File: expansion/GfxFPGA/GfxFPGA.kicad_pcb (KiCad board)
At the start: 4 copper layers, 100 x 100 mm, 3 parts, among them J1 JTAG, J101 D68K_64PIN_BOARD, J501 VGA Out

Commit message: WOrking on VGA card
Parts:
- removed J501: VGA Out, Connector_Dsub:DSUB-15-HD_Female_Horizontal_P2.29x1.98mm_EdgePinOffset3.03mm_Housed_MountingHolesOffset4.94mm
- added C1: 47uF, Capacitor_SMD:CP_Elec_4x5.3, F.Cu at (106.5, 99.5)
- added C10: 100nF, Capacitor_SMD:C_0805_2012Metric, B.Cu at (144.9, 94.3)
- added C11: 100nF, Capacitor_SMD:C_0805_2012Metric, B.Cu at (151.3, 100.7)
- added C12: 100nF, Capacitor_SMD:C_0805_2012Metric, B.Cu at (160.9, 93.4)
- added C13: 100nF, Capacitor_SMD:C_0805_2012Metric, B.Cu at (152.0, 84.7)
- added C14: 100nF, Capacitor_SMD:C_0805_2012Metric, B.Cu at (136.4, 116.3)
- added C15: 100nF, Capacitor_SMD:C_0805_2012Metric, B.Cu at (151.3, 96.4)
- added C16: 100nF, Capacitor_SMD:C_0805_2012Metric, B.Cu at (145.0, 89.4)
- added C17: 100nF, Capacitor_SMD:C_0805_2012Metric, B.Cu at (160.8, 88.6)
- added C18: 100nF, Capacitor_SMD:C_0805_2012Metric, B.Cu at (147.9, 84.8)
- added C19: 0.1uF, Capacitor_SMD:CP_Elec_4x5.3, F.Cu at (115.0, 92.9)
- added C2: 100nF, Capacitor_SMD:C_0805_2012Metric, F.Cu at (108.8, 116.6)
- added C20: 100nF, Capacitor_SMD:C_0805_2012Metric, B.Cu at (158.0, 84.7)
- added C21: 100nF, Capacitor_SMD:C_0805_2012Metric, B.Cu at (184.1, 128.7)
- added C22: 100nF, Capacitor_SMD:C_0805_2012Metric, B.Cu at (171.6, 129.1)
- added C23: 100nF, Capacitor_SMD:C_0805_2012Metric, B.Cu at (147.7, 115.8)
- added C24: 100nF, Capacitor_SMD:C_0805_2012Metric, B.Cu at (121.2, 128.8)
- added C25: 100nF, Capacitor_SMD:C_0805_2012Metric, B.Cu at (136.3, 122.7)
- added C26: 100nF, Capacitor_SMD:C_0805_2012Metric, B.Cu at (184.1, 132.4)
- added C27: 100nF, Capacitor_SMD:C_0805_2012Metric, B.Cu at (171.6, 132.4)
- added C28: 100nF, Capacitor_SMD:C_0805_2012Metric, B.Cu at (155.3, 129.8)
- added C29: 100nF, Capacitor_SMD:C_0805_2012Metric, B.Cu at (142.3, 129.9)
- added C3: 47uF, Capacitor_SMD:CP_Elec_4x5.3, F.Cu at (115.0, 99.6)
- added C30: 100nF, Capacitor_SMD:C_0805_2012Metric, B.Cu at (129.3, 129.8)
- added C31: 100nF, Capacitor_SMD:C_0805_2012Metric, B.Cu at (121.2, 132.7)
- added C32: 100nF, Capacitor_SMD:C_0805_2012Metric, B.Cu at (147.6, 119.6)
- added C33: 100nF, Capacitor_SMD:C_0805_2012Metric, B.Cu at (120.3, 73.0)
- added C34: 100nF, Capacitor_SMD:C_0805_2012Metric, B.Cu at (135.2, 72.9)
- added C35: 100nF, Capacitor_SMD:C_0805_2012Metric, F.Cu at (195.4, 116.3)
- added C36: 100nF, Capacitor_SMD:C_0805_2012Metric, F.Cu at (194.6, 79.7)
- added C37: 100nF, Capacitor_SMD:C_0805_2012Metric, F.Cu at (158.8, 115.9)
- added C4: 100nF, Capacitor_SMD:C_0805_2012Metric, F.Cu at (106.6, 103.4)
- added C5: 47uF, Capacitor_SMD:CP_Elec_4x5.3, F.Cu at (108.1, 123.5)
- added C6: 10uF, Capacitor_SMD:CP_Elec_4x5.3, F.Cu at (122.4, 111.8)
- added C7: 100nF, Capacitor_SMD:C_0805_2012Metric, F.Cu at (115.3, 103.4)
- added C8: 100nF, Capacitor_SMD:C_0805_2012Metric, F.Cu at (116.5, 110.0)
- added C9: 100nF, Capacitor_SMD:C_0805_2012Metric, F.Cu at (107.8, 135.6)
- added D1: LED, LED_SMD:LED_1206_3216Metric, F.Cu at (130.5, 98.7)
- added D2: LED, LED_SMD:LED_1206_3216Metric, F.Cu at (126.6, 98.7)
- added D3: LED, LED_SMD:LED_1206_3216Metric, F.Cu at (196.1, 130.6)
- added D4: LED, LED_SMD:LED_1206_3216Metric, F.Cu at (196.0, 133.6)
- added D5: LED, LED_SMD:LED_1206_3216Metric, F.Cu at (196.0, 127.6)
- added J3: DE15_Receptacle_HighDensity, Connector_Dsub:DSUB-15-HD_Female_Horizontal_P2.29x1.98mm_EdgePinOffset3.03mm_Housed_MountingHolesOffset4.94mm, F.Cu at (192.9, 93.6)
- added Q1: BC847, Package_TO_SOT_SMD:SOT-23, F.Cu at (122.4, 104.2)
- added R1: 390R, Resistor_SMD:R_0805_2012Metric, F.Cu at (126.9, 104.1)
- added R10: 0R, Resistor_SMD:R_0805_2012Metric, F.Cu at (185.1, 123.7)
- added R11: 0R, Resistor_SMD:R_0805_2012Metric, F.Cu at (168.5, 123.5)
- added R12: 0R, Resistor_SMD:R_0805_2012Metric, F.Cu at (166.1, 123.5)
- added R13: 0R, Resistor_SMD:R_0805_2012Metric, F.Cu at (192.7, 120.1)
- added R14: 10K, Resistor_SMD:R_0805_2012Metric, B.Cu at (159.8, 100.6)
- added R15: 10K, Resistor_SMD:R_0805_2012Metric, B.Cu at (155.7, 100.7)
- added R16: 10K, Resistor_SMD:R_0805_2012Metric, B.Cu at (146.7, 100.6)
- added R17: 10K, Resistor_SMD:R_0805_2012Metric, F.Cu at (108.8, 92.9)
- added R18: 390R, Resistor_SMD:R_0805_2012Metric, F.Cu at (192.7, 123.4)
- added R19: 10K, Resistor_SMD:R_0805_2012Metric, B.Cu at (164.4, 104.3)
- added R2: 390R, Resistor_SMD:R_0805_2012Metric, F.Cu at (130.4, 104.1)
- added R20: 10K, Resistor_SMD:R_0805_2012Metric, B.Cu at (180.0, 128.8)
- added R21: 499R, Resistor_SMD:R_0805_2012Metric, F.Cu at (187.5, 74.4)
- added R22: 1K, Resistor_SMD:R_0805_2012Metric, F.Cu at (187.5, 76.6)
- added R23: 2K, Resistor_SMD:R_0805_2012Metric, F.Cu at (187.5, 78.8)
- added R24: 4K, Resistor_SMD:R_0805_2012Metric, F.Cu at (187.5, 81.0)
- added R25: 8K, Resistor_SMD:R_0805_2012Metric, F.Cu at (187.5, 83.2)
- added R26: 499R, Resistor_SMD:R_0805_2012Metric, F.Cu at (187.5, 85.5)
- added R27: 1K, Resistor_SMD:R_0805_2012Metric, F.Cu at (187.5, 87.7)
- added R28: 2K, Resistor_SMD:R_0805_2012Metric, F.Cu at (187.5, 89.9)
- added R29: 4K, Resistor_SMD:R_0805_2012Metric, F.Cu at (187.5, 92.1)
- added R3: 390R, Resistor_SMD:R_0805_2012Metric, F.Cu at (122.3, 99.5)
- added R30: 8K, Resistor_SMD:R_0805_2012Metric, F.Cu at (187.5, 94.4)
- added R31: 16K, Resistor_SMD:R_0805_2012Metric, F.Cu at (187.5, 96.6)
- added R32: 499R, Resistor_SMD:R_0805_2012Metric, F.Cu at (187.4, 98.9)
- added R33: 1K, Resistor_SMD:R_0805_2012Metric, F.Cu at (187.4, 101.1)
- added R34: 2K, Resistor_SMD:R_0805_2012Metric, F.Cu at (187.4, 103.4)
- added R35: 4K, Resistor_SMD:R_0805_2012Metric, F.Cu at (187.4, 105.6)
- added R36: 8K, Resistor_SMD:R_0805_2012Metric, F.Cu at (187.3, 107.9)
- added R37: 82.5R, Resistor_SMD:R_0805_2012Metric, F.Cu at (187.4, 110.1)
- added R38: 82.5R, Resistor_SMD:R_0805_2012Metric, F.Cu at (187.4, 112.2)
- added R4: 120R, Resistor_SMD:R_0805_2012Metric, F.Cu at (116.6, 113.4)
- added R5: 390R, Resistor_SMD:R_0805_2012Metric, F.Cu at (196.7, 120.1)
- added R6: 390R, Resistor_SMD:R_0805_2012Metric, F.Cu at (196.6, 123.4)
- added R7: 10K, Resistor_SMD:R_0805_2012Metric, B.Cu at (132.3, 112.2)
- added R8: 10K, Resistor_SMD:R_0805_2012Metric, B.Cu at (136.8, 112.2)
- added R9: 10K, Resistor_SMD:R_0805_2012Metric, B.Cu at (141.4, 112.2)
- added U1: SN74LS125ADR, Package_SO:SO-14_3.9x8.65mm_P1.27mm, F.Cu at (110.7, 130.5)
- added U10: SN74LVC8T245PWR, Ddraig:SOP65P640X120-24N, F.Cu at (121.2, 130.3)
- added U11: SN74LVC8T245PWR, Ddraig:SOP65P640X120-24N, F.Cu at (182.2, 130.3)
- added U12: SN74LVC8T245PWR, Ddraig:SOP65P640X120-24N, F.Cu at (171.6, 130.3)
- added U13: IS61WV102416FBLL-10TLI, Ddraig:SOP50P2000X120-48N, F.Cu at (127.5, 72.8)
- added U2: LD1117S12TR_SOT223, Package_TO_SOT_SMD:SOT-223-3_TabPin2, F.Cu at (108.8, 111.5)
- added U3: XC6SLX9-TQG144, Ddraig:TQ144, F.Cu at (153.2, 93.1)
- added U4: W25Q64JVSSIM, Ddraig:SOIC127P790X195-8N, F.Cu at (136.4, 116.6)
- added U5: SN74LS157NSR, Package_SO:SO-16_5.3x10.2mm_P1.27mm, F.Cu at (145.7, 130.2)
- added U6: SN74LS157NSR, Package_SO:SO-16_5.3x10.2mm_P1.27mm, F.Cu at (158.4, 130.3)
- added U7: SN74LS157NSR, Package_SO:SO-16_5.3x10.2mm_P1.27mm, F.Cu at (133.1, 130.2)
- added U8: SN74LV1T34DBV, Package_TO_SOT_SMD:SOT-23-5, F.Cu at (136.3, 122.7)
- added U9: SN74LVC8T245PWR, Ddraig:SOP65P640X120-24N, F.Cu at (147.8, 117.2)
- added Y1: ECS-3963, Ddraig:OSC_ECS-3963, F.Cu at (155.5, 116.0)
- added Z1: ~, Ddraig:Ddraig68k-26mm, F.Cu at (149.9, 61.4)
- moved J2 15.9 mm to (165.0, 69.2)
- moved J1 0.10 mm to (189.0, 144.7)
- renumbered J101 to J1, J1 to J2
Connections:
- J1 pad C23: /CPU_CLK -> unconnected-(J1-SYS_CLK-PadC23)
- J2 pad 2: unconnected-(J1-Pin_2-Pad2) -> /FPGA/TCK
- J2 pad 3: unconnected-(J1-Pin_3-Pad3) -> /FPGA/TDI
- J2 pad 4: unconnected-(J1-Pin_4-Pad4) -> /FPGA/TDO
- J2 pad 5: unconnected-(J1-Pin_5-Pad5) -> /FPGA/TMS
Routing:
- net Net-(J3-Pad1): track 0.00 -> 22.6 mm
- net Net-(J3-Pad13): track 0.00 -> 20.8 mm, vias 0 -> 1
- net Net-(J3-Pad14): track 0.00 -> 20.6 mm
- net GND: track 0.00 -> 16.1 mm, vias 0 -> 6
- net Net-(J3-Pad2): track 0.00 -> 15.9 mm
- net Net-(J3-Pad3): track 0.00 -> 13.9 mm
- net Net-(D4-A): track 0.00 -> 12.1 mm
- net Net-(D3-A): track 0.00 -> 12.0 mm
- net +3V3: track 0.00 -> 11.0 mm, vias 0 -> 5
- net /FPGA/A7: track 0.00 -> 10.5 mm
- net /FPGA/A6: track 0.00 -> 10.4 mm
- net /FPGA/A5: track 0.00 -> 10.3 mm
- net /FPGA/A1: track 0.00 -> 10.3 mm
- net /FPGA/A4: track 0.00 -> 10.3 mm
- net /FPGA/A0: track 0.00 -> 10.2 mm
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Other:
- board text added: "+1V2"
- board text added: "+3V3"
- board text added: "ACTIVITY"
- board text added: "FLASH CS"
- board text added: "FPGA DONE"

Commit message: vga board update
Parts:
- moved R13 51.9 mm to (140.9, 122.6), turned to 90 degrees
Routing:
- net +3V3: track 11.0 -> 16.2 mm, vias 5 -> 6
- net GND: track 16.1 -> 19.1 mm, vias 6 -> 7
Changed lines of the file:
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@@
 	(footprint "Resistor_SMD:R_0805_2012Metric"
 		(layer "F.Cu")
-		(at 192.6863 120.0912)
+		(at 140.8938 122.6077 90)
 		(descr "Resistor SMD 0805 (2012 Metric), square (rectangular) end terminal, IPC_7351 nominal, (Body size source: IPC-SM-782 page 72, https://www.pcb-3d.com/wordpress/wp-content/uploads/ipc-sm-782a_amendment_1_and_2.pdf), generated with kicad-footprint-generator")
 		(tags "resistor")
 		(property "Reference" "R13"
-			(at 0 -1.65 0)
+			(at 0 -1.65 270)
 			(layer "F.SilkS")
 			(effects
@@
 		)
 		(property "Value" "0R"
-			(at 0 1.65 0)
+			(at 0 1.65 270)
 			(layer "F.Fab")
 			(effects
@@
 		)
 		(property "Footprint" "Resistor_SMD:R_0805_2012Metric"
-			(at 0 0 0)
+			(at 0 0 90)
 			(unlocked yes)
 			(layer "F.Fab")
@@
 		)
 		(property "Datasheet" ""
-			(at 0 0 0)
+			(at 0 0 90)
 			(unlocked yes)
 			(layer "F.Fab")
@@
 		)
 		(property "Description" "Resistor"
-			(at 0 0 0)
+			(at 0 0 90)
 			(unlocked yes)
 			(layer "F.Fab")
@@
 		)
 		(fp_line
-			(start -1.68 -0.95)
-			(end 1.68 -0.95)
+			(start 1.68 -0.95)
+			(end 1.68 0.95)
 			(stroke
 				(width 0.05)
@@
 		)
 		(fp_line
-			(start -1.68 0.95)
-			(end -1.68 -0.95)
+			(start -1.68 -0.95)
+			(end 1.68 -0.95)
 			(stroke
 				(width 0.05)
@@
 		)
 		(fp_line
-			(start 1.68 -0.95)
-			(end 1.68 0.95)
+			(start 1.68 0.95)
+			(end -1.68 0.95)
 			(stroke
 				(width 0.05)
@@
 		)
 		(fp_line
-			(start 1.68 0.95)
-			(end -1.68 0.95)
+			(start -1.68 0.95)
+			(end -1.68 -0.95)
 			(stroke
 				(width 0.05)
@@
 		)
 		(fp_line
-			(start -1 -0.625)
-			(end 1 -0.625)
+			(start 1 -0.625)
+			(end 1 0.625)
 			(stroke
 				(width 0.1)
@@
 		)
 		(fp_line
-			(start -1 0.625)
-			(end -1 -0.625)
+			(start -1 -0.625)
+			(end 1 -0.625)
 			(stroke
 				(width 0.1)
@@
 		)
 		(fp_line
-			(start 1 -0.625)
-			(end 1 0.625)
+			(start 1 0.625)
+			(end -1 0.625)
 			(stroke
 				(width 0.1)
@@
 		)
 		(fp_line
-			(start 1 0.625)
-			(end -1 0.625)
+			(start -1 0.625)
+			(end -1 -0.625)
 			(stroke
 				(width 0.1)
@@
 		)
 		(fp_text user "${REFERENCE}"
-			(at 0 0 0)
+			(at 0 0 270)
 			(layer "F.Fab")
 			(effects
@@
 		)
 		(pad "1" smd roundrect
-			(at -0.9125 0)
+			(at -0.9125 0 90)
 			(size 1.025 1.4)
 			(layers "F.Cu" "F.Paste" "F.Mask")
@@
 		)
 		(pad "2" smd roundrect
-			(at 0.9125 0)
+			(at 0.9125 0 90)
 			(size 1.025 1.4)
 			(layers "F.Cu" "F.Paste" "F.Mask")
@@
 	)
 	(segment
+		(start 157.5816 114.7318)
+		(end 156.5656 114.7318)
+		(width 0.254)
+		(layer "F.Cu")
+		(net 1)
+	)
+	(segment
 		(start 137.3124 72.581)
 		(end 135.8016 72.581)
@@
 	)
 	(segment
+		(start 158.75 114.3254)
+		(end 158.7246 114.3)
+		(width 0.254)
+		(layer "F.Cu")
+		(net 1)
+	)
+	(segment
+		(start 158.75 114.9858)
+		(end 158.75 114.3254)
+		(width 0.254)
+		(layer "F.Cu")
+		(net 1)
+	)
+	(segment
+		(start 157.8356 114.9858)
+		(end 157.5816 114.7318)
+		(width 0.254)
+		(layer "F.Cu")
+		(net 1)
+	)
+	(segment
+		(start 158.75 114.9858)
+		(end 157.8356 114.9858)
+		(width 0.254)
+		(layer "F.Cu")
+		(net 1)
+	)
+	(segment
 		(start 135.8016 72.581)
 		(end 135.2042 71.9836)
@@
 	)
 	(via
+		(at 158.7246 114.3)
+		(size 0.7)
+		(drill 0.4)
+		(layers "F.Cu" "B.Cu")
+		(net 1)
+	)
+	(via
 		(at 156.6164 99.7458)
 		(size 0.7)
@@
 	)
 	(segment
+		(start 156.5656 117.2718)
+		(end 157.1752 117.2718)
+		(width 0.254)
+		(layer "F.Cu")
+		(net 2)
+	)
+	(segment
 		(start 193.6648 79.6544)
 		(end 192.8114 79.6544)
@@
 	)
 	(segment
+		(start 158.75 117.5766)
+		(end 158.7246 117.602)
+		(width 0.254)
+		(layer "F.Cu")
+		(net 2)
+	)
+	(segment
 		(start 193.6242 116.332)
 		(end 193.5988 116.3066)
@@
 	)
 	(segment
+		(start 154.3656 117.2718)
+		(end 156.5656 117.2718)
+		(width 0.254)
+		(layer "F.Cu")
+		(net 2)
+	)
+	(segment
 		(start 192.8114 79.6544)
 		(end 192.786 79.629)
@@
 	)
 	(segment
+		(start 158.75 116.8858)
+		(end 158.75 117.5766)
+		(width 0.254)
+		(layer "F.Cu")
+		(net 2)
+	)
+	(segment
 		(start 136.0068 73.081)
 		(end 135.2042 73.8836)
@@
 	)
 	(segment
+		(start 157.5612 116.8858)
+		(end 158.75 116.8858)
+		(width 0.254)
+		(layer "F.Cu")
+		(net 2)
+	)
+	(segment
 		(start 146.9882 101.8556)
 		(end 147.5232 101.3206)
@@
 	)
 	(segment
+		(start 157.1752 117.2718)
+		(end 157.5612 116.8858)
+		(width 0.254)
+		(layer "F.Cu")
+		(net 2)
+	)
+	(segment
 		(start 146.9882 104.1656)
 		(end 146.9882 101.8556)
@@
 		(net 2)
 	)
+	(via
+		(at 158.7246 117.602)
+		(size 0.7)
+		(drill 0.4)
+		(layers "F.Cu" "B.Cu")
+		(net 2)
+	)

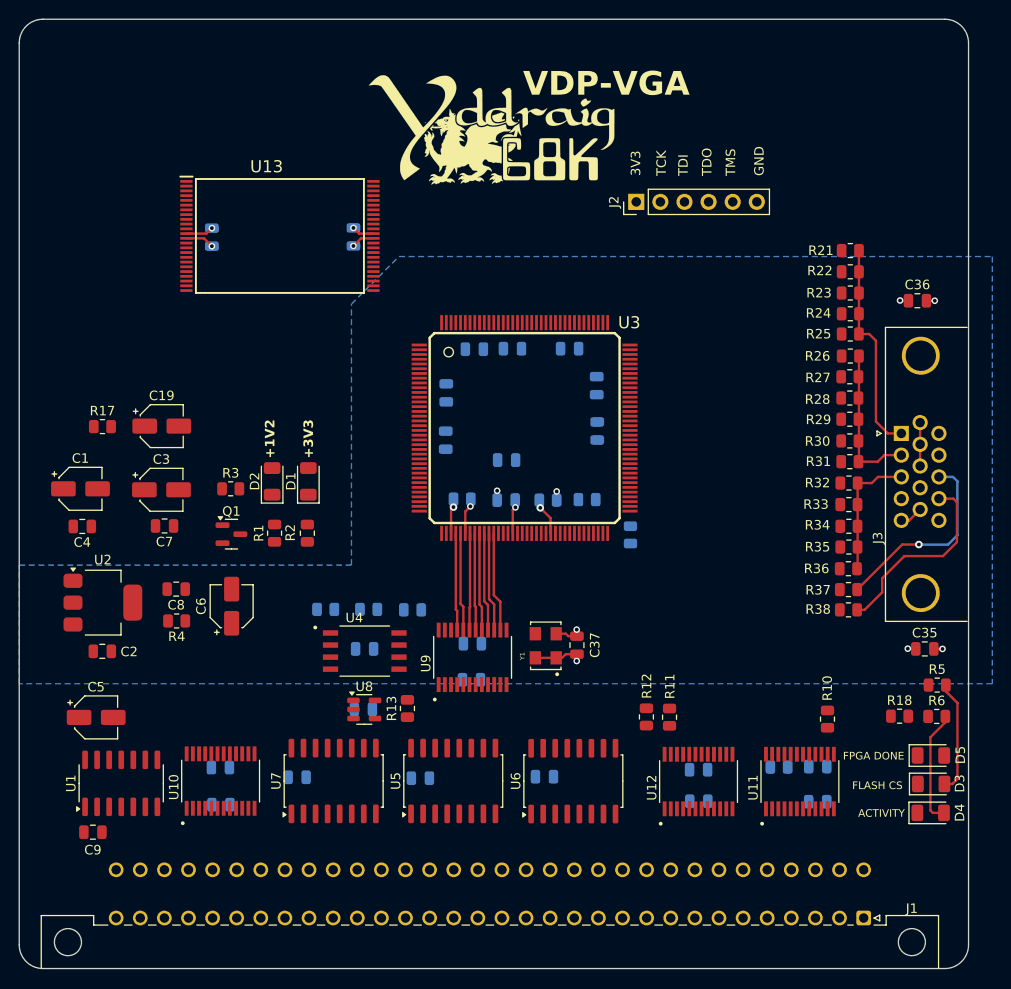
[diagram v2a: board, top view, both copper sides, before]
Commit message: Finished FPGA board layout
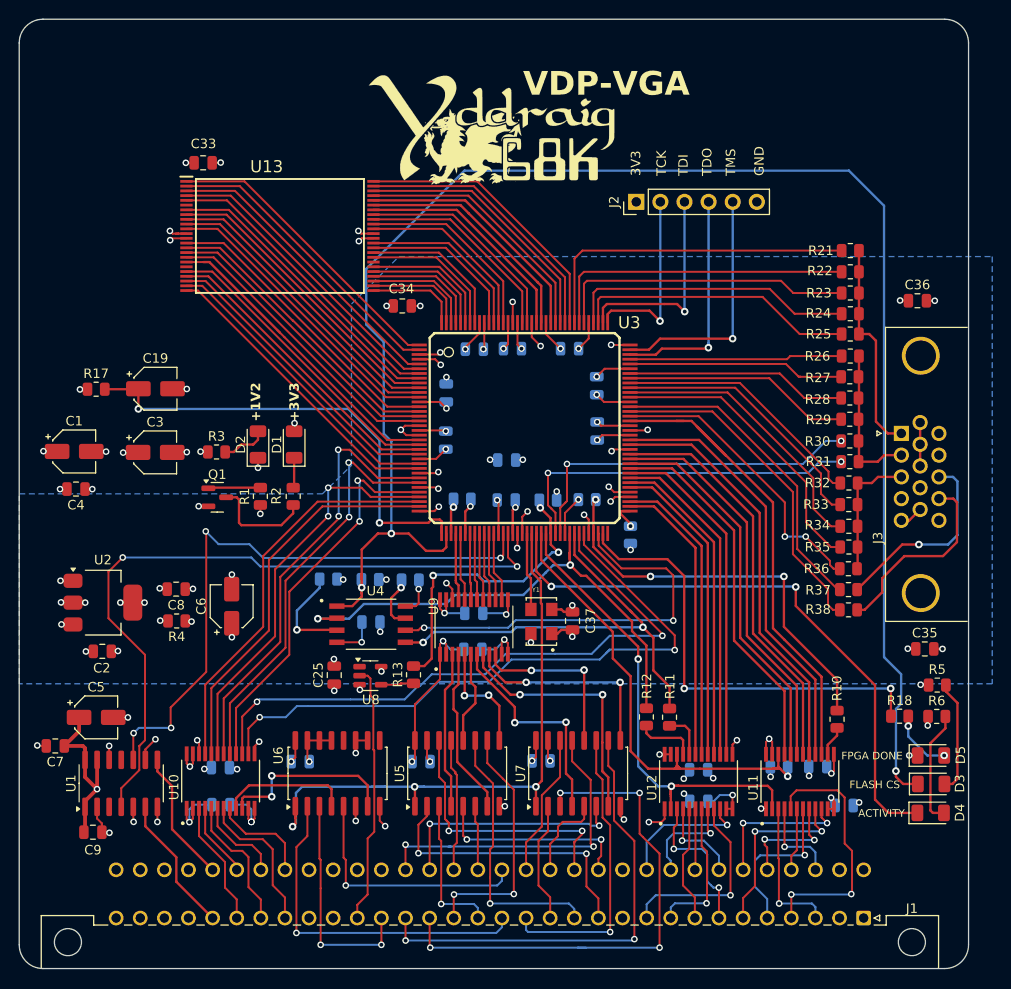
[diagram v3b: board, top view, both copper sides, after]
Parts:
- C25, C33, C34: moved to F.Cu
- moved C7 25.9 mm to (103.8, 126.5)
- moved U7 25.8 mm to (158.9, 129.4)
- moved U6 24.9 mm to (133.5, 129.4)
- moved C34 8.90 mm to (140.3, 80.2), turned to 180 degrees
- moved C33 7.89 mm to (119.4, 65.1), turned to 180 degrees
- moved C25 4.73 mm to (133.2, 119.1), turned to 90 degrees
- moved R2 4.16 mm to (128.9, 100.3)
- moved D2 4.16 mm to (125.2, 94.8)
- moved Q1 4.16 mm to (120.9, 100.4)
- moved D1 4.16 mm to (129.0, 94.8)
- moved R1 4.16 mm to (125.4, 100.3)
- moved R3 4.16 mm to (120.8, 95.6)
- moved C1 3.99 mm to (105.8, 95.5)
- moved C19 3.99 mm to (114.3, 88.9)
- moved C4 3.99 mm to (106.0, 99.5)
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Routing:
- net /FPGA/~{FLASH_CS}: track 0.00 -> 175.2 mm, vias 0 -> 3
- net GND: track 19.1 -> 146.4 mm, vias 7 -> 66
- net /~{CPU_IRQ}: track 0.00 -> 75.3 mm, vias 0 -> 2
- net +3V3: track 16.2 -> 89.5 mm, vias 6 -> 49
- net /FPGA/A9: track 0.00 -> 67.7 mm, vias 0 -> 2
- net /FPGA/A8: track 0.00 -> 66.1 mm, vias 0 -> 2
- net /FPGA/ADDR_MUX: track 0.00 -> 65.5 mm, vias 0 -> 3
- net /~{CPU_DTACK}: track 0.00 -> 64.2 mm, vias 0 -> 4
- net /FPGA/~{LED1}: track 0.00 -> 62.9 mm, vias 0 -> 2
- net /CPU_A15: track 0.00 -> 55.1 mm, vias 0 -> 4
- net +5V: track 0.00 -> 54.2 mm, vias 0 -> 10
- net /FPGA/FLASH_DO: track 0.00 -> 53.7 mm, vias 0 -> 2
- net /FPGA/D6: track 0.00 -> 52.3 mm
- net /FPGA/~{CPU_DATAEN}: track 0.00 -> 50.9 mm, vias 0 -> 1
- net /FPGA/FPGA_PROGB: track 0.00 -> 49.2 mm, vias 0 -> 2
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
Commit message: Gfx FPGA and V9990 gerber changes
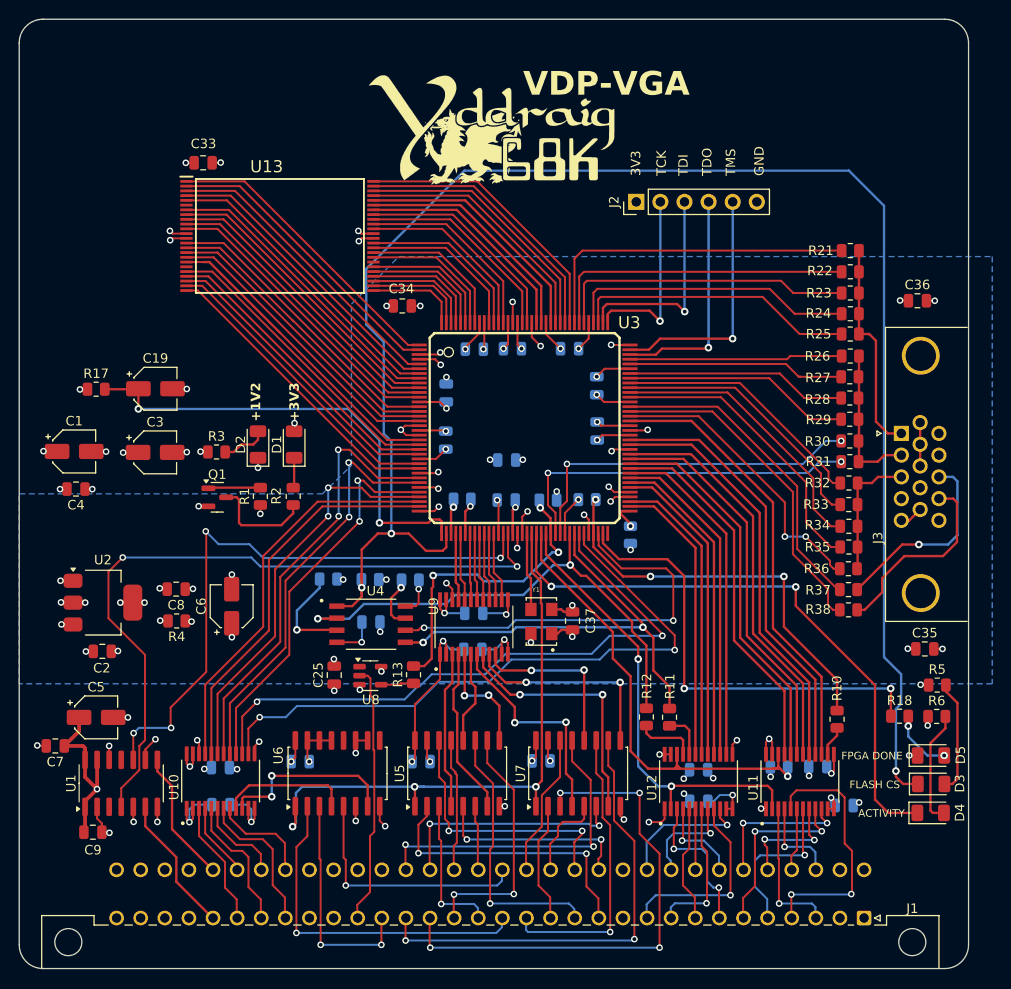
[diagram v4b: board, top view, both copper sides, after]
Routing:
- net /FPGA/D6: track 52.3 -> 47.3 mm
- net /FPGA/ADDR_MUX: track 65.5 -> 64.0 mm
- net +5V: track 54.2 -> 52.9 mm
- net /CPU_A15: track 55.1 -> 54.2 mm
- net /FPGA/FLASH_DO: track 53.7 -> 53.0 mm
- net /FPGA/DATA_DIR: track 48.8 -> 48.1 mm
- net /FPGA/~{SRAM_WE}: track 32.9 -> 32.3 mm
- net +3V3: track 89.5 -> 88.9 mm
- net /~{CPU_DATACS}: track 7.85 -> 7.34 mm
- net GND: track 146.4 -> 146.1 mm, vias 66 -> 65
